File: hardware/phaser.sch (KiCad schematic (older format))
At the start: 38 parts, among them IC1 STM32F042K4U6, IC2 MCP1700, P1 CONN_01X03, P2 SWD_TC, T1 230/6+6 1VA, U1 VTX-214-003-105

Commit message: part selection
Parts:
- removed C1, C8, C9: 1u, agg:0603, symbol C
- removed C3, C?: 4u7, agg:0603, symbol C
- removed C?: 100n, agg:0603, symbol C
- removed R1, R? (x3): R, agg:0603, symbol R
- removed R? (x2): R, symbol R
- added C?: 100n, agg:0603, symbol C
- added C? (x3): 1u, agg:0603, symbol C
- added C? (x2): 4u7, agg:0603, symbol C
- added IC?: AD8541, agg:SOT-23-5, symbol AD8541
- added Q? (x3): BSS138P, agg:SOT-23, symbol Q_NMOS_GSD
- added R? (x6): 10k, agg:0603, symbol R
- added R? (x2): 150, agg:0603, symbol R
- added R?: 50, agg:0603, symbol R
- added X?: FUSE, symbol PART
- C2: Farnell (none) -> 2496828
- C7: Farnell (none) -> 1198295
- C?: footprint (none) -> agg:0603; Farnell (none) -> 9227776
- C?: footprint (none) -> agg:0603; Farnell (none) -> 2496930
- D?: footprint (none) -> agg:SIL-254P-02; Farnell (none) -> 2431256
- D?: footprint (none) -> agg:SIL-254P-02; Farnell (none) -> 2431258
- D?: footprint (none) -> agg:SIL-254P-02; Farnell (none) -> 2431252
- F1: Farnell (none) -> 1162740
- P?: footprint (none) -> Connectors_JST:JST_PH_S2B-PH-K_02x2.00mm_Angled; Farnell (none) -> 9491902
- R?: footprint (none) -> agg:0603; Farnell (none) -> 2059468
- R?: footprint (none) -> agg:0603; Farnell (none) -> 2303162
- R?: value R -> 10k; footprint (none) -> agg:0603; Farnell (none) -> 9238603
- SW?: value SW_PUSH -> SW; footprint (none) -> agg:SIL-254P-02; Farnell (none) -> 1634622
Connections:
- net +3V3: now also C?.1, C?.1, C?.1, C?.1, IC?.5 (V+), R?.1, R?.2, R?.2
- net BATT_CHG: now also R?.2
- net GND: now also P?.2 (P2), C?.2, C?.2, C?.2, C?.2, C?.2, C?.2, IC?.2 (V-), Q?.2 (S), Q?.2 (S), Q?.2 (S), R?.1; no longer D?.1 (K), D?.1 (K), D?.1 (K), P?.1 (P1)
- net LED_B: now also Q?.1 (G); no longer D?.2 (A)
- net LED_R: now also Q?.1 (G); no longer D?.2 (A)
- net LED_Y: now also Q?.1 (G); no longer D?.2 (A)
- net PUSH_SW: now also R?.1
- net VSENSE: now also R?.1, R?.2
- net at T1.3 (SA): now also R?.2
- net at T1.4 (SB): now also IC?.1 (OUT), IC?.4 (-), R?.1
- net at C?.1, IC2.3 (VIN), IC?.10 (OUT)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: now also C?.1
- net at IC?.2 (BAT), IC?.3 (BAT): now also P?.1 (P1), C?.1; no longer P?.2 (P2)
- new net: D?.1 (K), Q?.3 (D) (x3)
- new net: D?.2 (A), R?.2 (x3)
- new net: IC?.3 (+), R?.1, R?.2
- new net +5V: R?.1, R?.1, R?.1
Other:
- moved on the sheet: C2, C4, C5, D?, SW?

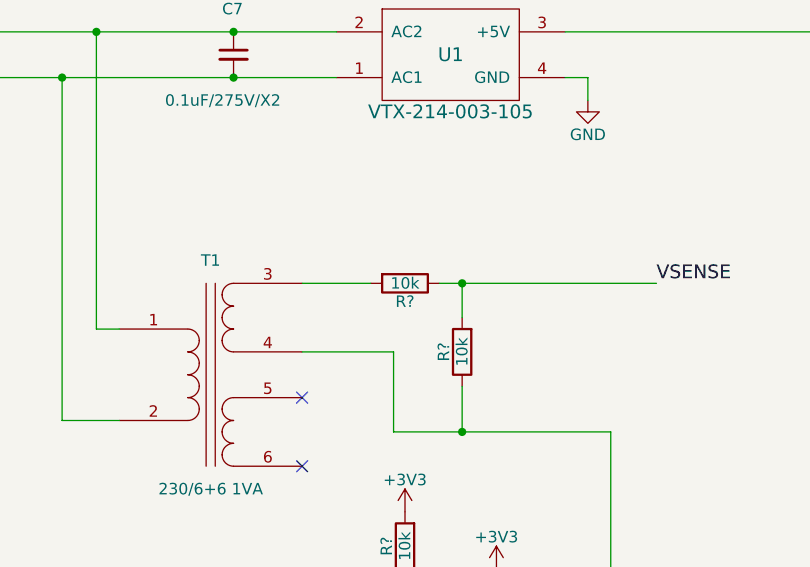
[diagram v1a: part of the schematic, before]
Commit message: Added footprints, bumped agg-kicad for bq24232
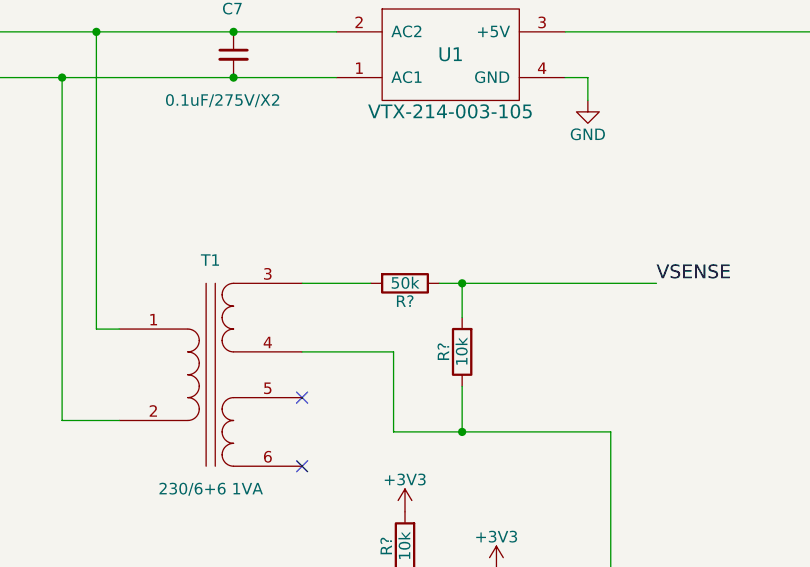
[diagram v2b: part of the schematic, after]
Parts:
- C7: footprint (none) -> footprints:ECQU2A104ML
- F1: footprint (none) -> footprints:5x20_clip
- R?: value 10k -> 50k; Farnell 9238603 -> (none)
- T1: footprint (none) -> footprints:VB1.0-2-6
- U1: footprint (none) -> footprints:VTX214
- U?: footprint (none) -> footprints:FOX924
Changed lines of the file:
@@
 F 0 "U1" H 3900 950 60  0000 C CNN
 F 1 "VTX-214-003-105" H 3900 700 60  0000 C CNN
-F 2 "" H 3900 950 60  0001 C CNN
+F 2 "footprints:VTX214" H 3900 950 60  0001 C CNN
 F 3 "http://www.farnell.com/datasheets/2060418.pdf" H 3900 950 60  0001 C CNN
 F 4 "2401030" H 3900 950 60  0001 C CNN "Farnell"
@@
 F 0 "T1" H 2850 2850 50  0000 C CNN
 F 1 "230/6+6 1VA" H 2850 1850 50  0000 C CNN
-F 2 "" H 2850 2350 50  0000 C CNN
-F 3 "" H 2850 2350 50  0000 C CNN
+F 2 "footprints:VB1.0-2-6" H 2850 2350 50  0001 C CNN
+F 3 "http://www.farnell.com/datasheets/65263.pdf" H 2850 2350 50  0001 C CNN
 F 4 "1131622" H 2850 2350 60  0001 C CNN "Farnell"
 	1    2850 2350
@@
 F 0 "C7" H 2900 1150 50  0000 L CNN
 F 1 "0.1uF/275V/X2" H 2650 750 50  0000 L CNN
-F 2 "" H 2950 950 50  0001 C CNN
+F 2 "footprints:ECQU2A104ML" H 2950 950 50  0001 C CNN
 F 3 "http://www.farnell.com/datasheets/2059979.pdf" H 2950 950 50  0001 C CNN
 F 4 "1198295" H 2950 950 60  0001 C CNN "Farnell"
@@
 F 0 "F1" H 1360 910 50  0000 L CNN
 F 1 "100mA TD" H 1200 800 50  0000 L CNN
-F 2 "" H 1400 850 50  0000 C CNN
+F 2 "footprints:5x20_clip" H 1400 850 50  0001 C CNN
 F 3 "http://www.farnell.com/datasheets/2020897.pdf" H 1400 850 50  0001 C CNN
 F 4 "1162740" H 1400 850 60  0001 C CNN "Farnell"
@@
 F 0 "U?" V 2150 5400 60  0000 C CNN
 F 1 "FOX924B-20.000" H 2150 5200 60  0000 C CNN
-F 2 "" H 2100 5300 60  0001 C CNN
+F 2 "footprints:FOX924" H 2100 5300 60  0001 C CNN
 F 3 "http://www.farnell.com/datasheets/1465427.pdf" H 2100 5300 60  0001 C CNN
 F 4 "2063961" H 2150 5400 60  0001 C CNN "Farnell"
@@
 P 3700 1950
 F 0 "R?" V 3780 1950 50  0000 C CNN
-F 1 "10k" V 3700 1950 50  0000 C CNN
+F 1 "50k" V 3700 1950 50  0000 C CNN
 F 2 "agg:0603" V 3630 1950 50  0001 C CNN
-F 3 "http://www.farnell.com/datasheets/1868787.pdf" H 3700 1950 50  0001 C CNN
-F 4 "9238603" H 3700 1950 60  0001 C CNN "Farnell"
+F 3 "" H 3700 1950 50  0001 C CNN
 	1    3700 1950
 	0    1    1    0

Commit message: Parts and rough board outlines
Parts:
- removed P1: CONN_01X03, symbol CONN_01X03
- removed R? (x2): 150, agg:0603, symbol R
- removed R?: 50, agg:0603, symbol R
- added C7: 100n, agg:0603, symbol C
- added IC3: LMx93, agg:SOIC-8, symbol LMx93
- added P1: L, agg:SIL-254P-01, symbol CONN_01X01
- added P3: COAX, agg:SMA-EDGE, symbol COAX
- added P5: N, agg:SIL-254P-01, symbol CONN_01X01
- added R10, R11, R9: 68, agg:0603, symbol R
- added SW2: CLK_SRC, agg:SIL-254P-03, symbol SWITCH_INV
- P2: renamed from P?; footprint Connectors_JST:JST_PH_S2B-PH-K_02x2.00mm_Angled -> footprints:JST-PH-2
- gave numbers to parts that had none: 31
- renumbered C7 to C1, C4 to C11, C5 to C12, C2 to C9, IC2 to IC1, IC1 to IC5, P2 to P4
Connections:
- net +3V3: now also C7.2, IC3.8 (VCC), R10.1, R9.1
- net +5V: now also R11.1
- net GND: now also C7.1, IC3.4 (GND), IC3.5 (2IN+), IC3.6 (2IN-), P3.2 (GND)
- net N: now also P5.1 (P1)
- net VSENSE: now also IC3.3 (1IN+)
- net at F1.2: now also P1.1 (P1)
- net VSENSE_REF: now reaches IC4.1 (OUT), IC4.4 (-), R6.1, T1.4 (SB)
- net VSENSE_REF: now also IC3.2 (1IN-)
- net at IC5.2 (PF0): now also SW2.2; no longer U2.3 (OUT)
- net at D1.2 (A): now also R9.2
- net at D2.2 (A): now also R10.2
- net at D3.2 (A): now also R11.2
- new net: SW2.3, U2.3 (OUT)
- new net: P3.1 (RF), SW2.1
- new net VSENSE_COMP: IC3.1 (1OUT)
- no-connect marks 10 -> 11
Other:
- note added: "Note different supply voltages!\nBlue needs the extra volts but\nwe can light red/yellow from battery"
- moved on the sheet: C10, C11, C12, C13, C14, C4, C5, C8, C9, IC1, IC4, IC5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
